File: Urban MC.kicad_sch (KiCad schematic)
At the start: 84 parts, among them J1 CAN, J2 CAN, J4 Conn_02x02_CUSTOM, J5 Conn_01x02, J6 Conn_01x03, J7 Conn_01x15_Socket, J8 Conn_02x03_CUSTOM, Q1 IQE022N06LM5CGSCATMA1, Q10 IQE022N06LM5CGSCATMA1, Q11 IQE022N06LM5CGSCATMA1, Q12 IQE022N06LM5CGSCATMA1, Q13 IQE022N06LM5CGSCATMA1, Q14 IQE022N06LM5CGSCATMA1, Q15 IQE022N06LM5CGSCATMA1, Q16 IQE022N06LM5CGSCATMA1, Q17 IQE022N06LM5CGSCATMA1, Q18 IQE022N06LM5CGSCATMA1, Q19 IQE022N06LM5CGSCATMA1, Q2 IQE022N06LM5CGSCATMA1, Q20 IQE022N06LM5CGSCATMA1, Q21 IQE022N06LM5CGSCATMA1, Q22 IQE022N06LM5CGSCATMA1, Q23 IQE022N06LM5CGSCATMA1, Q24 IQE022N06LM5CGSCATMA1, Q3 IQE022N06LM5CGSCATMA1, Q4 IQE022N06LM5CGSCATMA1, Q5 IQE022N06LM5CGSCATMA1, Q6 IQE022N06LM5CGSCATMA1, Q7 IQE022N06LM5CGSCATMA1, Q8 IQE022N06LM5CGSCATMA1, Q9 IQE022N06LM5CGSCATMA1, SW1 CAN_TERM, SW2 SW_Push, U1 MCP2561/2, U2 MCP4725, U3 MCP2515-xSO, Y1 8MHz

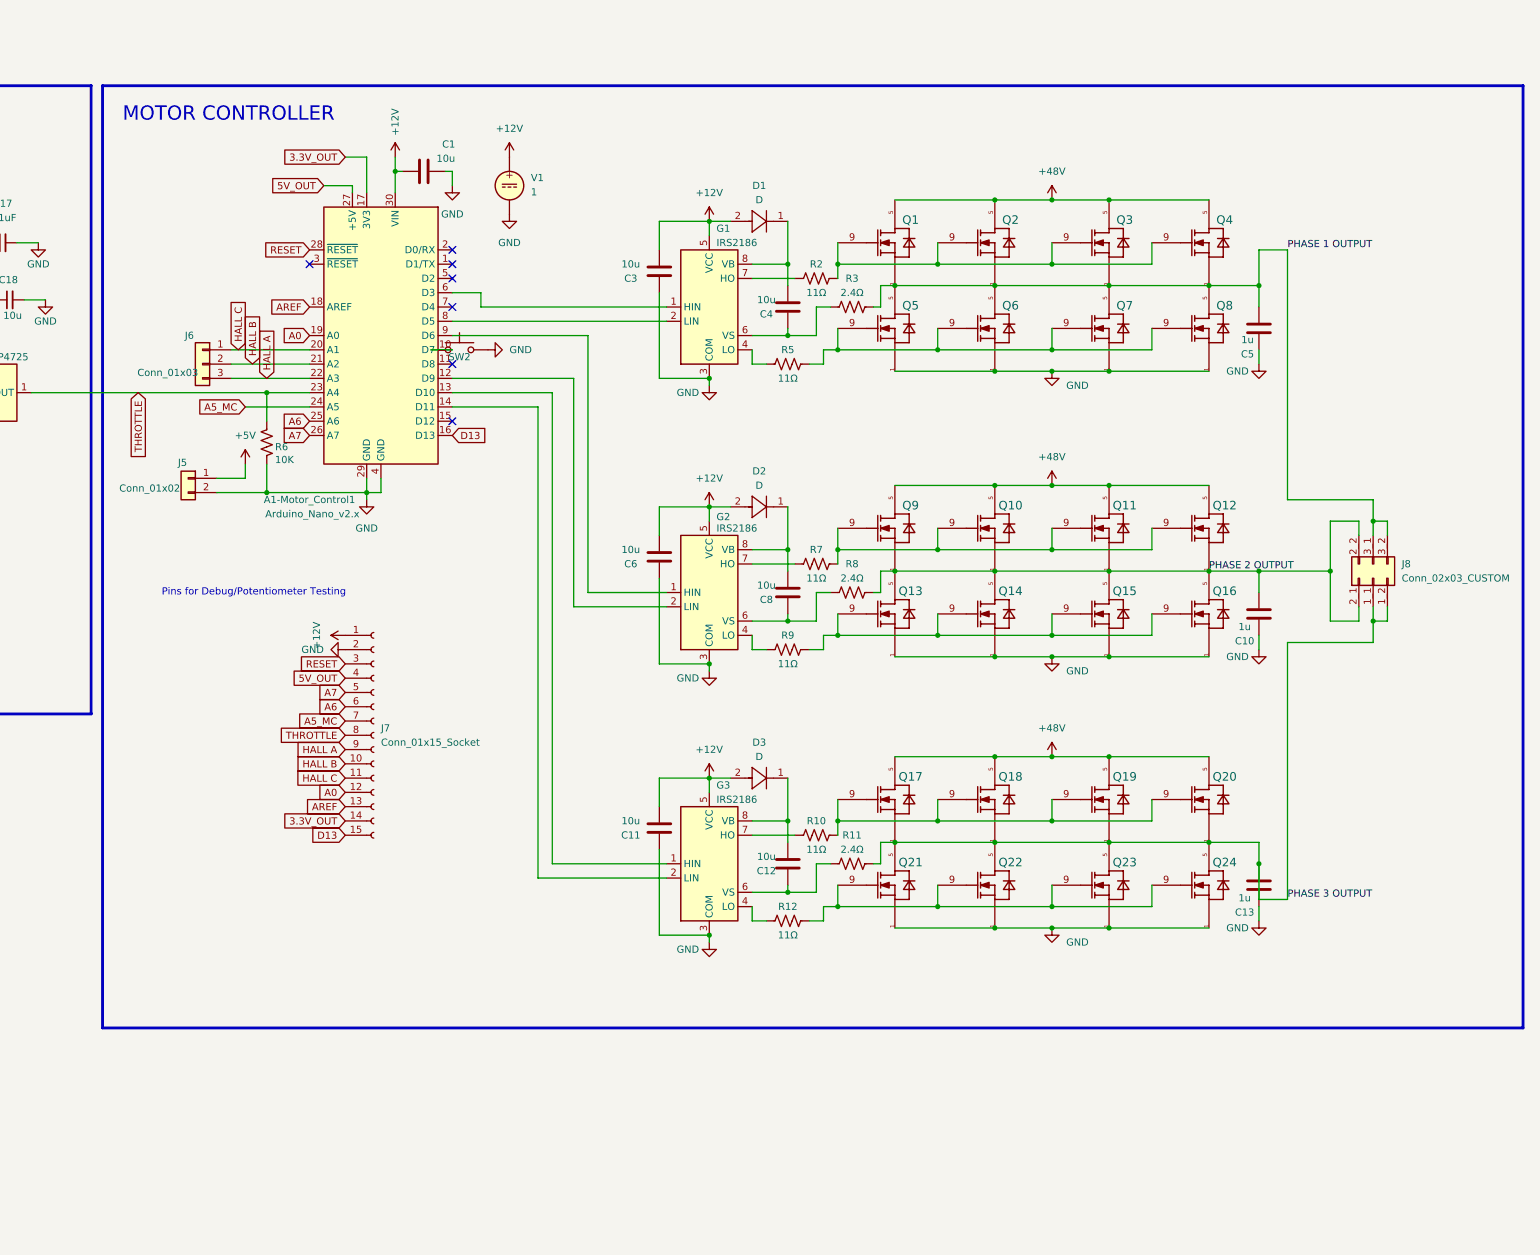
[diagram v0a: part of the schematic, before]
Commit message: Layout almost complete, just need to add vias
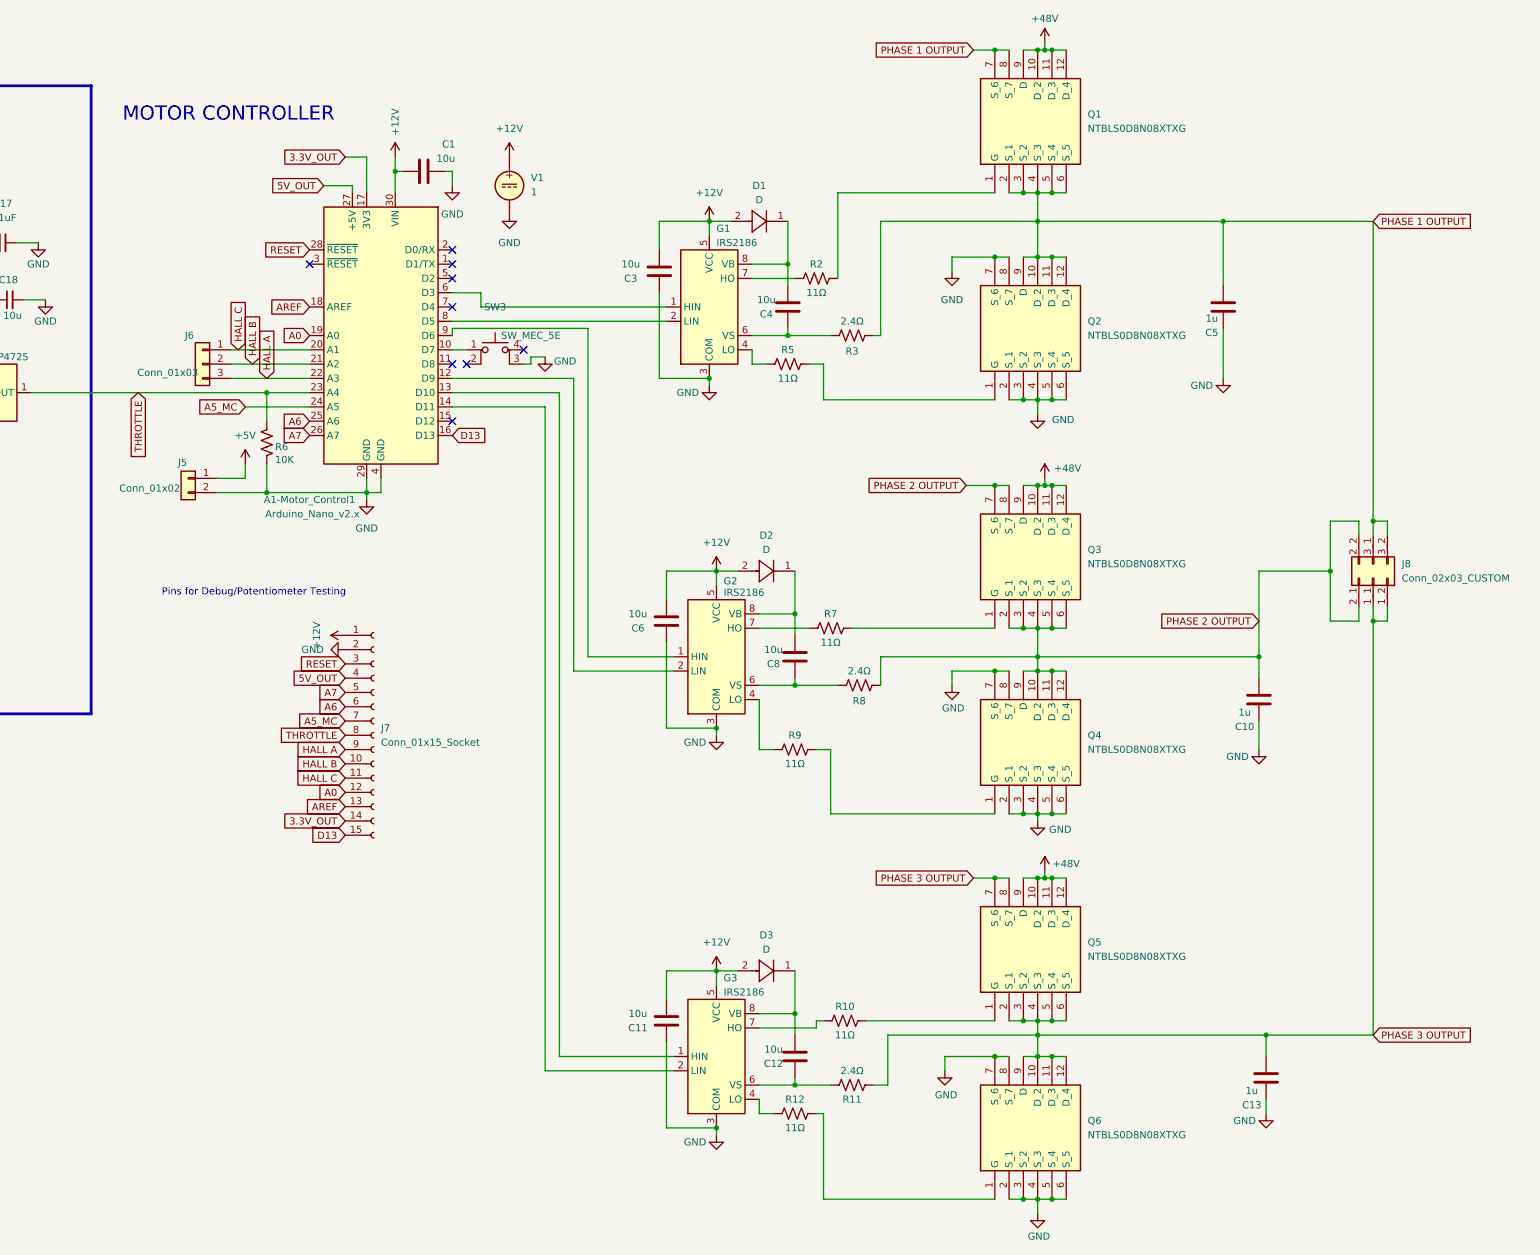
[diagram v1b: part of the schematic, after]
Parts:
- removed Q1, Q10, Q11, Q12, Q13, Q14, Q15, Q16, Q17, Q18, Q19, Q2, Q20, Q21, Q22, Q23, Q24, Q3, Q4, Q5, Q6, Q7, Q8, Q9: IQE022N06LM5CGSCATMA1, urban_mc_custom_footprints:IFX-PG-WHTFN-9-1-V, symbol Supermileage Symbols:root_0_IQE022N06LM5CGSC
- removed SW2: SW_Push, urban_mc_custom_footprints:SW_TS04-66-70-BK-160-SMT, symbol Switch:SW_Push
- added Q1, Q2, Q3, Q4, Q5, Q6: NTBLS0D8N08XTXG, urban_mc_custom_footprints:NVBLS1D1N08H, symbol NTBLS0D8N08XTXG:NTBLS0D8N08XTXG
- added SW3: SW_MEC_5E, urban_mc_custom_footprints:SW_TS04-66-70-BK-160-SMT, symbol Switch:SW_MEC_5E
- J4: footprint (none) -> urban_mc_custom_footprints:TE_1-1986660-2
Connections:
- net +48V: now also Q1.10 (D_2), Q1.11 (D_3), Q1.12 (D_4), Q1.9 (D), Q3.10 (D_2), Q3.11 (D_3), Q3.12 (D_4), Q3.9 (D), Q5.10 (D_2), Q5.11 (D_3), Q5.12 (D_4), Q5.9 (D)
- net GND: now also Q2.2 (S_1), Q2.3 (S_2), Q2.4 (S_3), Q2.5 (S_4), Q2.6 (S_5), Q2.7 (S_6), Q2.8 (S_7), Q4.2 (S_1), Q4.3 (S_2), Q4.4 (S_3), Q4.5 (S_4), Q4.6 (S_5), Q4.7 (S_6), Q4.8 (S_7), Q6.2 (S_1), Q6.3 (S_2), Q6.4 (S_3), Q6.5 (S_4), Q6.6 (S_5), Q6.7 (S_6), Q6.8 (S_7), SW3.3 (K)
- net PHASE 1 OUTPUT: now also Q1.2 (S_1), Q1.3 (S_2), Q1.4 (S_3), Q1.5 (S_4), Q1.6 (S_5), Q1.7 (S_6), Q1.8 (S_7), Q2.10 (D_2), Q2.11 (D_3), Q2.12 (D_4), Q2.9 (D)
- net PHASE 2 OUTPUT: now also Q3.2 (S_1), Q3.3 (S_2), Q3.4 (S_3), Q3.5 (S_4), Q3.6 (S_5), Q3.7 (S_6), Q3.8 (S_7), Q4.10 (D_2), Q4.11 (D_3), Q4.12 (D_4), Q4.9 (D)
- net PHASE 3 OUTPUT: now also Q5.2 (S_1), Q5.3 (S_2), Q5.4 (S_3), Q5.5 (S_4), Q5.6 (S_5), Q5.7 (S_6), Q5.8 (S_7), Q6.10 (D_2), Q6.11 (D_3), Q6.12 (D_4), Q6.9 (D)
- net at R5.2: now also Q2.1 (G)
- net at R12.2: now also Q6.1 (G)
- net at R10.2: now also Q5.1 (G)
- net at A1-Motor_Control1.10 (D7): now also SW3.1
- net at R7.2: now also Q3.1 (G)
- net at R9.2: now also Q4.1 (G)
- net at R2.2: now also Q1.1 (G)
- no-connect marks 35 -> 37
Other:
- moved on the sheet: C10, C11, C12, C13, C5, C6, C8, D2, D3, G2, G3, R10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

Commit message: design review changes in progress
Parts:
- added C19: 1m, urban_mc_custom_footprints:CAPPRD750W80D1600H2500, symbol Device:C
- added D5: D_TVS, urban_mc_custom_footprints:PTVS1058CH, symbol Device:D_TVS
- C14: value 10u -> 1m; footprint Capacitor_SMD:C_0805_2012Metric -> urban_mc_custom_footprints:CAPPRD750W80D1600H2500
- J4: value Conn_02x02_CUSTOM -> VBAT
- TP_48V0: footprint TestPoint:TestPoint_Pad_2.5x2.5mm -> TestPoint:TestPoint_THTPad_D1.0mm_Drill0.5mm
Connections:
- net +48V: now also C19.1, D5.2 (A2)
- net GND: now also C19.2, D5.1 (A1)
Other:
- moved on the sheet: J4

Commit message: Design Review Changes (WIP)
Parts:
- removed C14, C19: 1m, urban_mc_custom_footprints:CAPPRD750W80D1600H2500, symbol Device:C
- added C14: 1m, urban_mc_custom_footprints:CAPPRD750W80D1600H2500, symbol Device:C_Polarized
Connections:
- net +48V: now also C14.1
- net GND: now also C14.2
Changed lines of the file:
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@@
 	)
 	(junction
-		(at 58.42 187.96)
-		(diameter 0)
-		(color 0 0 0 0)
-	)
-	(junction
 		(at 355.6 199.39)
 		(diameter 0)
@@
 	)
 	(junction
-		(at 58.42 172.72)
-		(diameter 0)
-		(color 0 0 0 0)
-	)
-	(junction
 		(at 215.9 105.41)
 		(diameter 0)
@@
 	(wire
 		(pts
-			(xy 58.42 172.72) (xy 59.69 172.72)
-		)
-		(stroke
-			(width 0)
-			(type default)
-		)
-	)
-	(wire
-		(pts
 			(xy 35.56 59.69) (xy 44.45 59.69)
 		)
@@
 	(wire
 		(pts
-			(xy 57.15 172.72) (xy 58.42 172.72)
+			(xy 57.15 172.72) (xy 59.69 172.72)
 		)
 		(stroke
@@
 	(wire
 		(pts
-			(xy 58.42 172.72) (xy 58.42 176.53)
-		)
-		(stroke
-			(width 0)
-			(type default)
-		)
-	)
-	(wire
-		(pts
 			(xy 353.06 129.54) (xy 353.06 134.62)
 		)
@@
 	(wire
 		(pts
-			(xy 57.15 187.96) (xy 58.42 187.96)
+			(xy 57.15 187.96) (xy 67.31 187.96)
 		)
 		(stroke
@@
 	(wire
 		(pts
-			(xy 58.42 187.96) (xy 67.31 187.96)
-		)
-		(stroke
-			(width 0)
-			(type default)
-		)
-	)
-	(wire
-		(pts
 			(xy 86.36 99.06) (xy 86.36 90.17)
 		)
@@
 	(wire
 		(pts
-			(xy 58.42 184.15) (xy 58.42 187.96)
-		)
-		(stroke
-			(width 0)
-			(type default)
-		)
-	)
-	(wire
-		(pts
 			(xy 86.36 90.17) (xy 38.1 90.17)
 		)
@@
 	)
 	(symbol
+		(lib_id "Device:C_Polarized")
+		(at 52.07 180.34 0)
+		(unit 1)
+		(exclude_from_sim no)
+		(in_bom yes)
+		(on_board yes)
+		(dnp no)
+		(property "Reference" "C14"
+			(at 54.356 178.054 0)
+			(effects
+				(font
+					(size 1.27 1.27)
+				)
+				(justify left)
+			)
+		)
+		(property "Value" "1m"
+			(at 54.864 182.626 0)
+			(effects
+				(font
+					(size 1.27 1.27)
+				)
+				(justify left)
+			)
+		)
+		(property "Footprint" "urban_mc_custom_footprints:CAPPRD750W80D1600H2500"
+			(at 53.0352 184.15 0)
+			(effects
+				(font
+					(size 1.27 1.27)
+				)
+				(hide yes)
+			)
+		)
+		(property "Datasheet" "https://www.bourns.com/docs/Product-Datasheets/PTVS1-xxxC-H.pdf"
+			(at 52.07 180.34 0)
+			(effects
+				(font
+					(size 1.27 1.27)
+				)
+				(hide yes)
+			)
+		)
+		(property "Description" "Polarized capacitor"
+			(at 52.07 180.34 0)
+			(effects
+				(font
+					(size 1.27 1.27)
+				)
+				(hide yes)
+			)
+		)
+		(pin "2"
+		)
+		(pin "1"
+		)
+		(instances
+			(project ""
+				(path "/9c188f5e-4c43-43bc-b719-7c7a34d1ae77"
+					(reference "C14")
+					(unit 1)
+				)
+			)
+		)
+	)
+	(symbol
 		(lib_id "power:+12V")
 		(at 118.11 172.72 270)
@@
 	)
 	(symbol
-		(lib_id "Device:C")
-		(at 52.07 180.34 0)
-		(unit 1)
-		(exclude_from_sim no)
-		(in_bom yes)
-		(on_board yes)
-		(dnp no)
-		(property "Reference" "C14"
-			(at 48.006 177.546 0)
-			(effects
-				(font
-					(size 1.27 1.27)
-				)
-				(justify left)
-			)
-		)
-		(property "Value" "1m"
-			(at 48.26 182.626 0)
-			(effects
-				(font
-					(size 1.27 1.27)
-				)
-				(justify left)
-			)
-		)
-		(property "Footprint" "urban_mc_custom_footprints:CAPPRD750W80D1600H2500"
-			(at 53.0352 184.15 0)
-			(effects
-				(font
-					(size 1.27 1.27)
-				)
-				(hide yes)
-			)
-		)
-		(property "Datasheet" "https://industrial.panasonic.com/cdbs/www-data/pdf/RDE0000/RDE0000C1255.pdf"
-			(at 52.07 180.34 0)
-			(effects
-				(font
-					(size 1.27 1.27)
-				)
-				(hide yes)
-			)
-		)
-		(property "Description" "Unpolarized capacitor"
-			(at 52.07 180.34 0)
-			(effects
-				(font
-					(size 1.27 1.27)
-				)
-				(hide yes)
-			)
-		)
-		(pin "1"
-		)
-		(pin "2"
-		)
-		(instances
-			(project "Urban MC"
-				(path "/9c188f5e-4c43-43bc-b719-7c7a34d1ae77"
-					(reference "C14")
-					(unit 1)
-				)
-			)
-		)
-	)
-	(symbol
 		(lib_id "Device:C_Small")
 		(at 33.02 119.38 90)
@@
 					(unit 1)
 				)
-			)
-		)
-	)
-	(symbol
-		(lib_id "Device:C")
-		(at 58.42 180.34 0)
-		(unit 1)
-		(exclude_from_sim no)
-		(in_bom yes)
-		(on_board yes)
-		(dnp no)
-		(property "Reference" "C19"
-			(at 58.674 177.546 0)
-			(effects
-				(font
-					(size 1.27 1.27)
-				)
-				(justify left)
-			)
-		)
-		(property "Value" "1m"
-			(at 59.182 182.626 0)
-			(effects
-				(font
-					(size 1.27 1.27)
-				)
-				(justify left)
-			)
-		)
-		(property "Footprint" "urban_mc_custom_footprints:CAPPRD750W80D1600H2500"
-			(at 59.3852 184.15 0)
-			(effects
-				(font
-					(size 1.27 1.27)
-				)
-				(hide yes)
-			)
-		)
-		(property "Datasheet" "https://industrial.panasonic.com/cdbs/www-data/pdf/RDE0000/RDE0000C1255.pdf"
-			(at 58.42 180.34 0)
-			(effects
-				(font
-					(size 1.27 1.27)
-				)
-				(hide yes)
-			)
-		)
-		(property "Description" "Unpolarized capacitor"
-			(at 58.42 180.34 0)
-			(effects
-				(font
-					(size 1.27 1.27)
-				)
-				(hide yes)
-			)
-		)
-		(pin "1"
-		)
-		(pin "2"
-		)
-		(instances
-			(project "Urban MC"
-				(path "/9c188f5e-4c43-43bc-b719-7c7a34d1ae77"
-					(reference "C19")
-					(unit 1)
-				)

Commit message: all post-design review changes except vias
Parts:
- removed J1, J2: CAN, urban_mc_custom_footprints:CONN_70553-xxxx_03_MOL, symbol Connector_Generic:Conn_01x03
- added C19, C20, C21: 4.7 uF, Capacitor_SMD:C_1210_3225Metric, symbol Device:C
- added D6, D7: LED, LED_SMD:LED_0805_2012Metric, symbol Device:LED
- added J1: CAN, urban_mc_custom_footprints:CONN_5569-04A_MOL, symbol Connector_Generic:Conn_02x02_Counter_Clockwise
- added R16: 4.7k, Resistor_SMD:R_0805_2012Metric, symbol Device:R_US
- added R17: 1.5k, Resistor_SMD:R_0805_2012Metric, symbol Device:R_US
- C10, C13, C5: value 1u -> 4.7 uF; footprint Capacitor_SMD:C_2220_5750Metric -> Capacitor_SMD:C_1210_3225Metric
- TP_12V0, TP_5V0: footprint TestPoint:TestPoint_Pad_2.5x2.5mm -> TestPoint:TestPoint_THTPad_D2.0mm_Drill1.0mm
- TP_48V0: footprint TestPoint:TestPoint_THTPad_D1.0mm_Drill0.5mm -> TestPoint:TestPoint_THTPad_D2.0mm_Drill1.0mm
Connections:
- net +12V: now also R16.1
- net +48V: now also C10.1, C13.1, C5.1, C19.1, C20.1, C21.1
- net CAN HIGH: now also J1.1 (Pin_1), J1.3 (Pin_3)
- net CAN LOW: now also J1.2 (Pin_2), J1.4 (Pin_4)
- net GND: now also C10.2, C13.2, C5.2, C19.2, C20.2, C21.2, D6.1 (K), D7.1 (K); no longer C10.1, C13.1, C5.1
- net PHASE 1 OUTPUT: no longer C5.2
- net PHASE 2 OUTPUT: no longer C10.2
- net PHASE 3 OUTPUT: no longer C13.2
- net at A2-CAN1.2 (D0/RX): now also R17.1
- new net: D6.2 (A), R16.2
- new net: D7.2 (A), R17.2
- no-connect marks 37 -> 36
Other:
- note added: "Phase 1 LOCAL DC-Link Caps"
- note added: "Phase 2 LOCAL DC-Link Caps"
- note added: "Phase 3 LOCAL DC-Link Caps"

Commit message: V1.2 ORDERED VERSION
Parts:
- renumbered SW3 to SW2
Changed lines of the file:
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@@
 			)
 		)
-		(property "Datasheet" "~"
+		(property "Datasheet" "https://www.samsungsem.com/resources/file/global/support/product_catalog/MLCC_Automotive.pdf"
 			(at 388.62 71.12 0)
 			(effects
@@
 			)
 		)
-		(property "Datasheet" "SSB44-E3/52T"
+		(property "Datasheet" "https://www.vishay.com/docs/88884/ssb43l.pdf"
 			(at 299.72 119.38 0)
 			(effects
@@
 			)
 		)
-		(property "Datasheet" "SSB44-E3/52T"
+		(property "Datasheet" "https://www.vishay.com/docs/88884/ssb43l.pdf"
 			(at 298.45 57.15 0)
 			(effects
@@
 			)
 		)
-		(property "Datasheet" "~"
+		(property "Datasheet" "https://www.samsungsem.com/resources/file/global/support/product_catalog/MLCC_Automotive.pdf"
 			(at 400.05 147.32 0)
 			(effects
@@
 			)
 		)
-		(property "Datasheet" "~"
+		(property "Datasheet" "https://www.samsungsem.com/resources/file/global/support/product_catalog/MLCC_Automotive.pdf"
 			(at 398.78 71.12 0)
 			(effects
@@
 			)
 		)
-		(property "Datasheet" "~"
+		(property "Datasheet" "https://www.samsungsem.com/resources/file/global/support/product_catalog/MLCC_Automotive.pdf"
 			(at 389.89 147.32 0)
 			(effects
@@
 		(on_board yes)
 		(dnp no)
-		(property "Reference" "SW3"
-			(at 256.54 72.39 0)
+		(property "Reference" "SW2"
+			(at 256.54 83.312 0)
 			(effects
 				(font
@@
 			(project ""
 				(path "/9c188f5e-4c43-43bc-b719-7c7a34d1ae77"
-					(reference "SW3")
+					(reference "SW2")
 					(unit 1)
 				)
@@
 			)
 		)
-		(property "Datasheet" "~"
+		(property "Datasheet" "https://www.samsungsem.com/resources/file/global/support/product_catalog/MLCC_Automotive.pdf"
 			(at 391.16 215.9 0)
 			(effects
@@
 			)
 		)
-		(property "Datasheet" "~"
+		(property "Datasheet" "https://www.samsungsem.com/resources/file/global/support/product_catalog/MLCC_Automotive.pdf"
 			(at 401.32 215.9 0)
 			(effects
